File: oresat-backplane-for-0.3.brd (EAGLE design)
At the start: 83 x 214 mm, 3 parts, among them X1 87758-4416, X2 87758-4416, X3 87758-4416

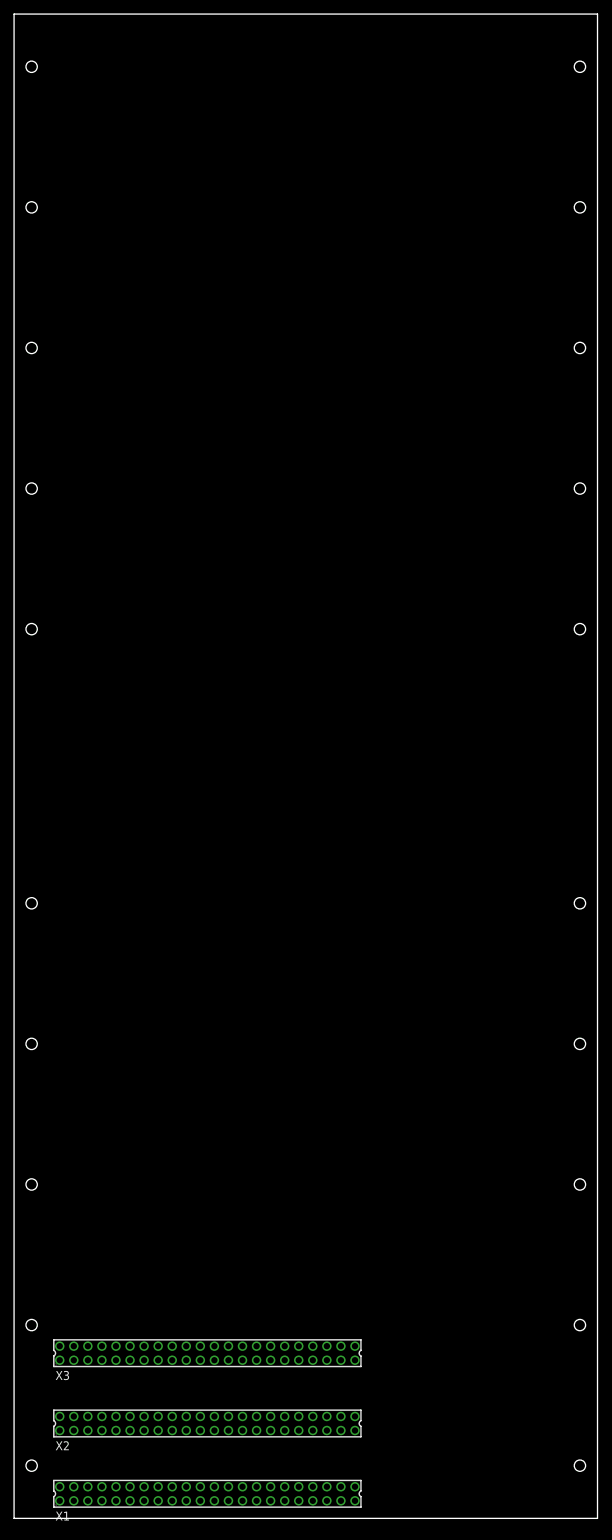
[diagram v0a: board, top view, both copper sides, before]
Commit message: Updated backplane to latest connectors - 1.27 mm 2x20 and new MCX connectors. Also added keep outs from Jeremy.
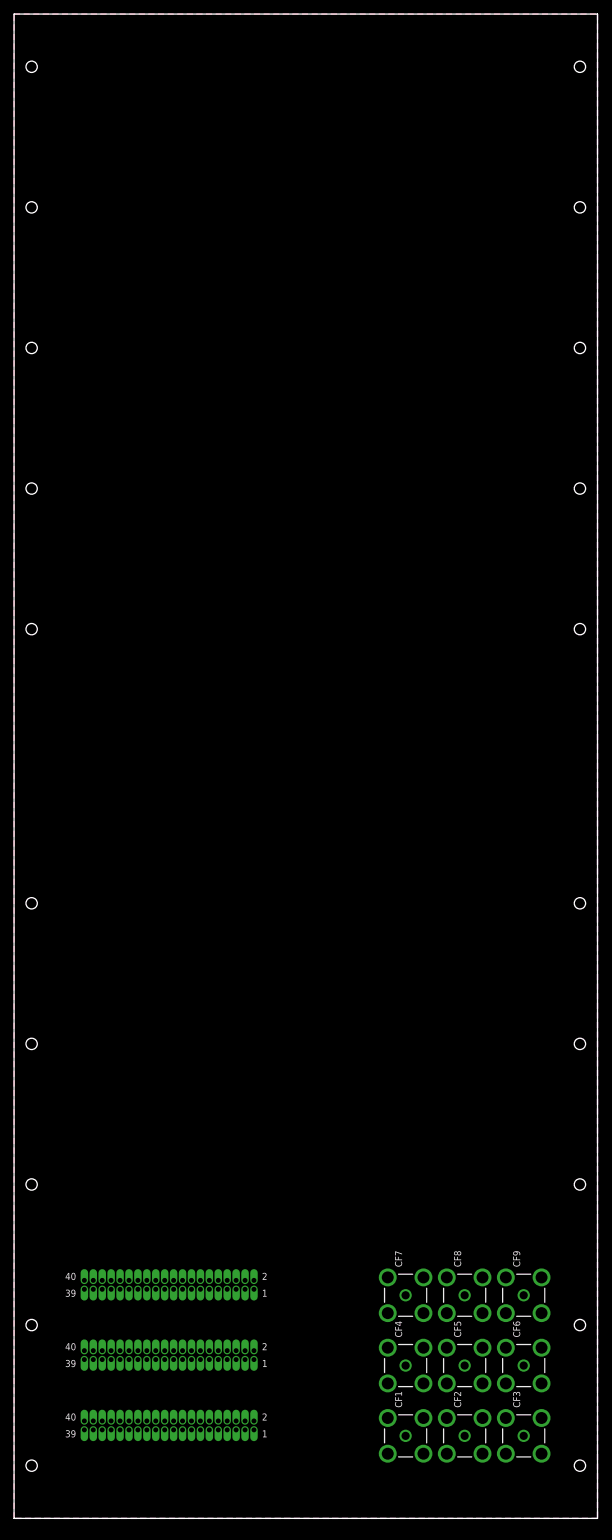
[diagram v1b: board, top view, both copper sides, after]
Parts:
- removed X1, X2, X3: 87758-4416, con-molex:87758-4416
- added CF1, CF2, CF3, CF4, CF5, CF6, CF7, CF8, CF9: ORESAT-RF-BACKPLANE, oresat-eagle:CON-MCX-F-CINCH-133-3801-201
- added CM1, CM2, CM3: ORESAT-BACKPLANE-40PIN, oresat-eagle:HARWIN-ARCHER-M50-3502042
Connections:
- new net GND: CF1.SHEILD2, CF1.SHEILD3, CF1.SHEILD4, CF1.SHIELD1, CF2.SHEILD2, CF2.SHEILD3, CF2.SHEILD4, CF2.SHIELD1, CF3.SHEILD2, CF3.SHEILD3, CF3.SHEILD4, CF3.SHIELD1, CF4.SHEILD2, CF4.SHEILD3, CF4.SHEILD4, CF4.SHIELD1, CF5.SHEILD2, CF5.SHEILD3, CF5.SHEILD4, CF5.SHIELD1, CF6.SHEILD2, CF6.SHEILD3, CF6.SHEILD4, CF6.SHIELD1, CF7.SHEILD2, CF7.SHEILD3, CF7.SHEILD4, CF7.SHIELD1, CF8.SHEILD2, CF8.SHEILD3, CF8.SHEILD4, CF8.SHIELD1, CF9.SHEILD2, CF9.SHEILD3, CF9.SHEILD4, CF9.SHIELD1
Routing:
- added copper zone on layer 1, net GND
- added copper zone on layer 16, net GND

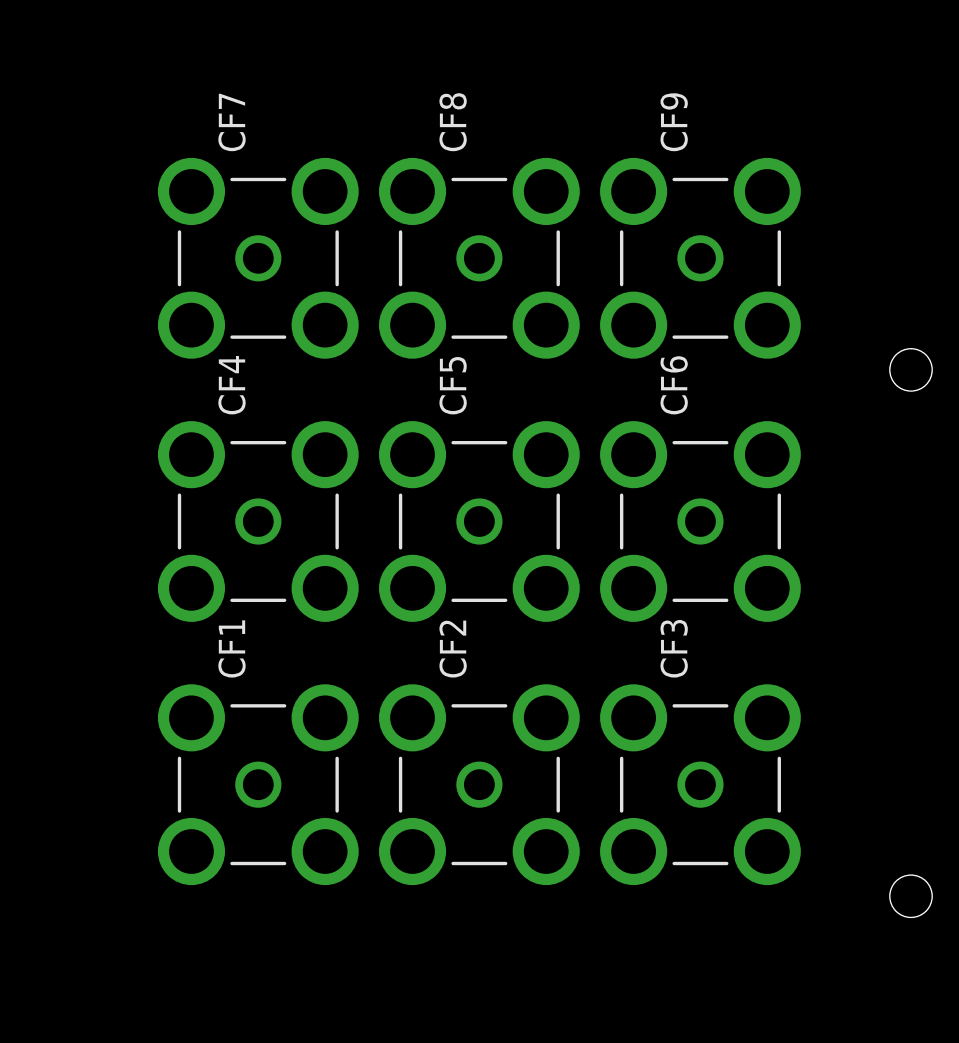
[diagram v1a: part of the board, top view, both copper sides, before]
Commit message: Updated to TE MCX M verticals to save precious, precious mm on the cards
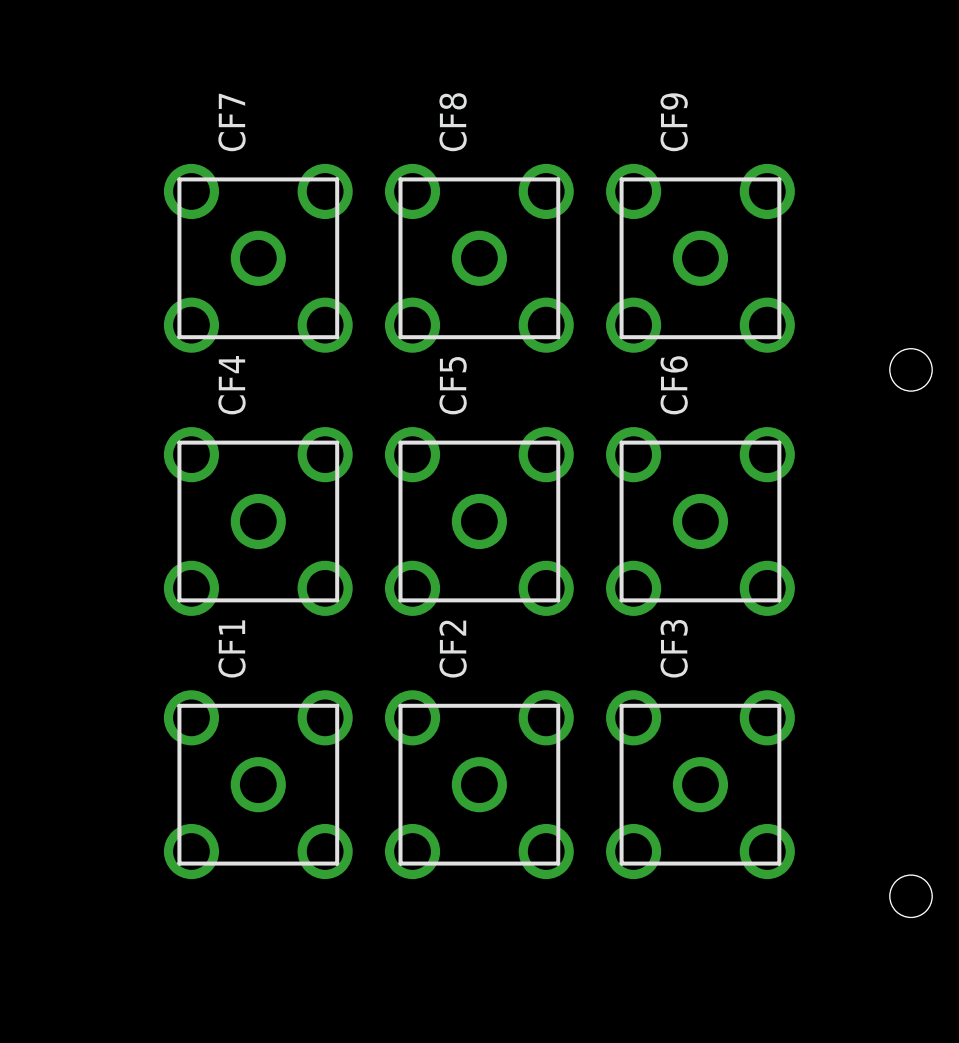
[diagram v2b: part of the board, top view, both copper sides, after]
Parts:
- CF1, CF2, CF3, CF4, CF5, CF6, CF7, CF8, CF9: value ORESAT-RF-BACKPLANE -> CON-MCX-M-TE-1061015-1; device oresat-eagle:CON-MCX-F-CINCH-133-3801-201 -> oresat-eagle:CONN_1061015-1_TYCO
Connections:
- net GND: now also CF1.SHIELD2, CF1.SHIELD3, CF1.SHIELD4, CF2.SHIELD2, CF2.SHIELD3, CF2.SHIELD4, CF3.SHIELD2, CF3.SHIELD3, CF3.SHIELD4, CF4.SHIELD2, CF4.SHIELD3, CF4.SHIELD4, CF5.SHIELD2, CF5.SHIELD3, CF5.SHIELD4, CF6.SHIELD2, CF6.SHIELD3, CF6.SHIELD4, CF7.SHIELD2, CF7.SHIELD3, CF7.SHIELD4, CF8.SHIELD2, CF8.SHIELD3, CF8.SHIELD4, CF9.SHIELD2, CF9.SHIELD3, CF9.SHIELD4; no longer CF1.SHEILD2, CF1.SHEILD3, CF1.SHEILD4, CF2.SHEILD2, CF2.SHEILD3, CF2.SHEILD4, CF3.SHEILD2, CF3.SHEILD3, CF3.SHEILD4, CF4.SHEILD2, CF4.SHEILD3, CF4.SHEILD4, CF5.SHEILD2, CF5.SHEILD3, CF5.SHEILD4, CF6.SHEILD2, CF6.SHEILD3, CF6.SHEILD4, CF7.SHEILD2, CF7.SHEILD3, CF7.SHEILD4, CF8.SHEILD2, CF8.SHEILD3, CF8.SHEILD4, CF9.SHEILD2, CF9.SHEILD3, CF9.SHEILD4
